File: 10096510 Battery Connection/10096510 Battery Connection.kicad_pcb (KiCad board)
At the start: 4 copper layers, 0 parts

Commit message: Replace 10096510 Battery Connection.kicad_pcb
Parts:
- added C1: 10nF, Capacitor_SMD:C_0603_1608Metric, B.Cu at (143.0, 104.5)
- added C2: 10nF, Capacitor_SMD:C_0603_1608Metric, B.Cu at (127.0, 104.5)
- added C3: 47pF, Capacitor_SMD:C_0603_1608Metric, B.Cu at (123.5, 94.5)
- added C4: 47pF, Capacitor_SMD:C_0603_1608Metric, B.Cu at (127.0, 94.5)
- added FI2: Ferrite bead, Resistor_SMD:R_0603_1608Metric, B.Cu at (123.5, 89.0)
- added FI3: Ferrite bead, Resistor_SMD:R_0603_1608Metric, B.Cu at (127.0, 89.0)
- added FL1: BNX002-01, myParts:BNX002-01, F.Cu at (135.5, 104.0)
- added J1: Conn_02x05_Odd_Even, Connector_IDC:IDC-Header_2x05_P2.54mm_Horizontal, F.Cu at (137.0, 92.0)
- added J3: +, myParts:811S100230014101, B.Cu at (108.7, 103.0)
- added J4: BAT_EEPROM, myParts:811S100230014101, B.Cu at (108.7, 107.0)
- added J5: T, myParts:811S100230014101, B.Cu at (108.7, 111.0)
- added J6: GND, myParts:GKS-913-Z, B.Cu at (108.7, 115.0)
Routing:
- net Net-(C2-Pad2): track 0.00 -> 55.4 mm
- net Net-(C2-Pad1): track 0.00 -> 51.5 mm
- net Net-(C4-Pad1): track 0.00 -> 41.8 mm
- net Net-(C1-Pad1): track 0.00 -> 29.9 mm
- net Net-(C3-Pad1): track 0.00 -> 25.5 mm
- net Net-(C1-Pad2): track 0.00 -> 22.5 mm
- net Net-(FI2-Pad2): track 0.00 -> 20.1 mm
- net Net-(FI3-Pad2): track 0.00 -> 17.0 mm
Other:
- board outline added: 68 x 45 mm
- net class HIGH CURRENT added: clearance 0.1524, trace_width 2, via_dia 0.6858, via_drill 0.3302
- board text added: "Battery Connection RB0505 10096506 Rev A"

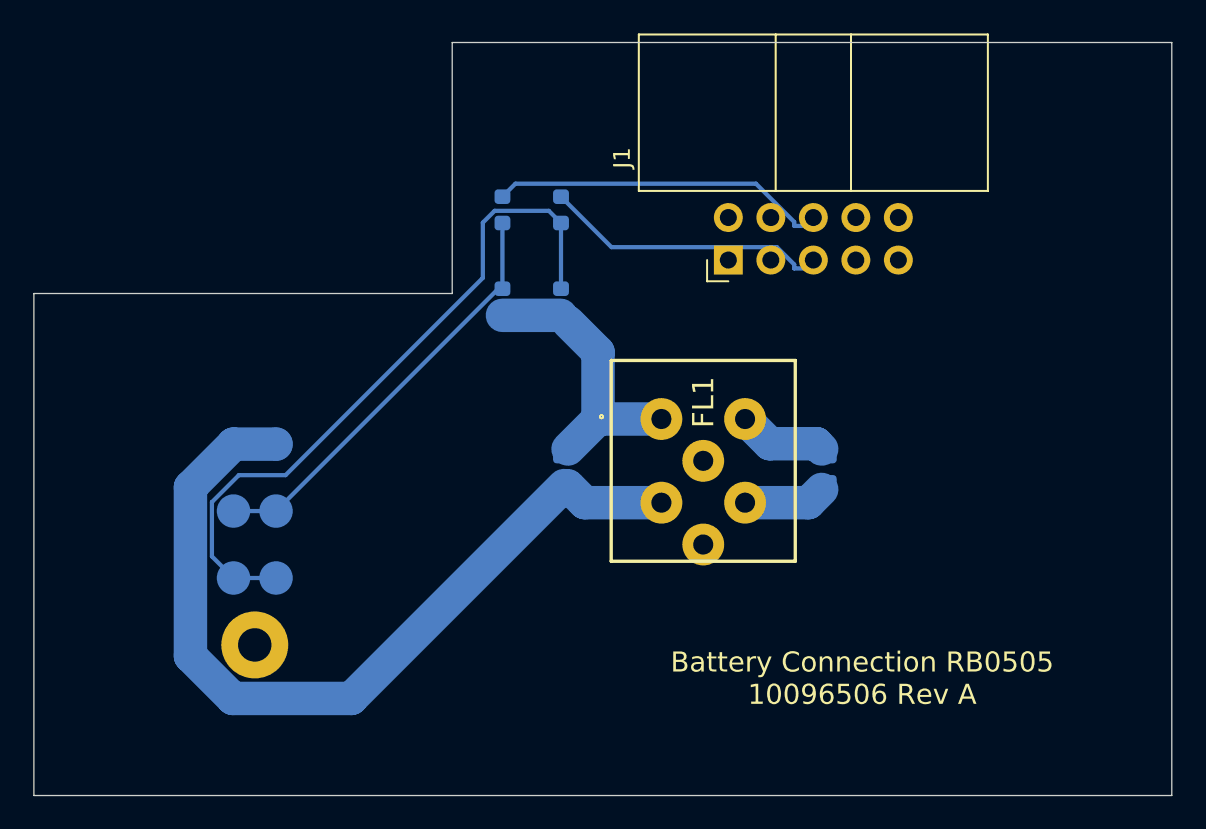
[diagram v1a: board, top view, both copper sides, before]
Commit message: Fixed missing pin 6 on BNX002-11 symbol. Updated footprint to match existing layout pin configuration for BNX002-11. Aligned components to placement on current design. Started routing. Layout still work in progress.
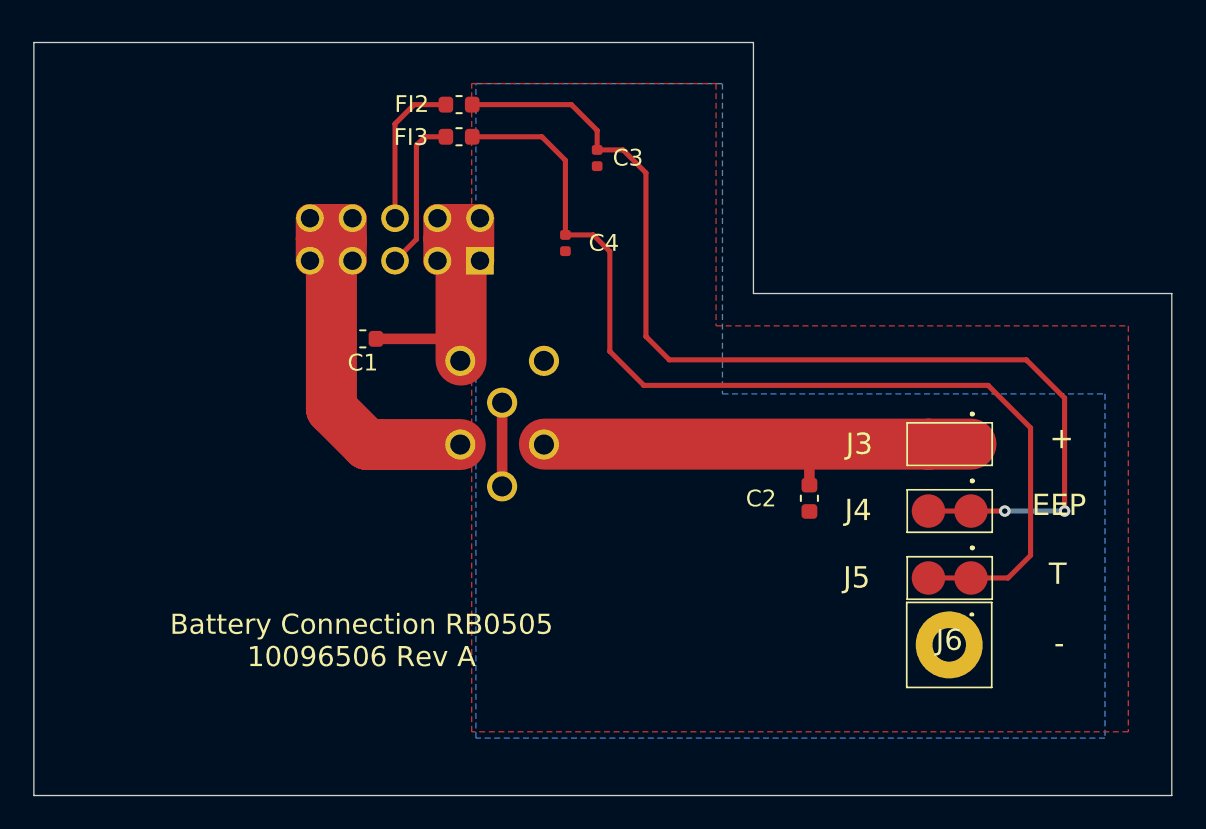
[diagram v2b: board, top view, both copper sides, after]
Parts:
- removed FL1: BNX002-01, myParts:BNX002-01
- added FI1: BNX002-11, 10096510 Battery Connection:BNX002-011, B.Cu at (123.5, 100.5)
- C1, C2: footprint Capacitor_SMD:C_0603_1608Metric -> 10096510 Battery Connection:C_0603_1608Metric; moved to F.Cu
- C3, C4: value 47pF -> 0402_47pF_C0402C470J5GAC; footprint Capacitor_SMD:C_0603_1608Metric -> 10096510 Battery Connection:C_0402_1005Metric; moved to F.Cu
- FI2, FI3: value Ferrite bead -> 74279266; footprint Resistor_SMD:R_0603_1608Metric -> 10096510 Battery Connection:L_0603_1608Metric; moved to F.Cu
- J1: value Conn_02x05_Odd_Even -> 09185107323; footprint Connector_IDC:IDC-Header_2x05_P2.54mm_Horizontal -> 10096510 Battery Connection:SHDRRA10W64P254_2X5_2050X890X930P; moved to B.Cu
- J3: value + -> 811-S1-002-30-014101; footprint myParts:811S100230014101 -> 10096510 Battery Connection:CONN_811S100230014101; moved to F.Cu
- J4: value BAT_EEPROM -> 811-S1-002-30-014101; footprint myParts:811S100230014101 -> 10096510 Battery Connection:CONN_811S100230014101; moved to F.Cu
- J5: value T -> 811-S1-002-30-014101; footprint myParts:811S100230014101 -> 10096510 Battery Connection:CONN_811S100230014101; moved to F.Cu
- J6: value GND -> GKS-913-0024; footprint myParts:GKS-913-Z -> 10096510 Battery Connection:CONN_GKS-913-Z; moved to F.Cu
- moved J3 41.5 mm to (150.2, 103.0), turned to 180 degrees
- moved J4 41.5 mm to (150.2, 107.0), turned to 180 degrees
- moved J5 41.5 mm to (150.2, 111.0), turned to 180 degrees
- moved J6 41.5 mm to (150.2, 115.0), turned to 180 degrees
- moved C1 28.9 mm to (115.2, 96.7), turned to 180 degrees
- moved C2 14.9 mm to (141.8, 106.2), turned to 270 degrees
- moved J1 14.8 mm to (122.2, 92.0), turned to 180 degrees
- moved C3 10.3 mm to (129.2, 85.9)
- moved FI3 7.50 mm to (120.9, 84.6), turned to 0 degrees
- moved FI2 6.80 mm to (120.9, 82.7), turned to 180 degrees
- moved C4 3.53 mm to (127.3, 91.0)
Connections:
- net Net-(C2-Pad1) renamed /+
- net Net-(C2-Pad2) renamed GND
- net Net-(C3-Pad1) renamed /BAT_EEPROM
- C1 pad 1: Net-(C1-Pad1) -> Earth
- C1 pad 2: Net-(C1-Pad2) -> VDD
- C4 pad 1: Net-(C4-Pad1) -> /T
- FI3 pad 1: Net-(C4-Pad1) -> Net-(FI3-Pad1)
- FI3 pad 2: Net-(FI3-Pad2) -> /T
- J1 pad 1: Net-(C1-Pad2) -> Earth
- J1 pad 10: Net-(C1-Pad1) -> VDD
- J1 pad 2: Net-(C1-Pad2) -> Earth
- J1 pad 3: Net-(C1-Pad2) -> Earth
- J1 pad 4: Net-(C1-Pad2) -> Earth
- J1 pad 5: Net-(FI3-Pad2) -> Net-(FI3-Pad1)
- J1 pad 7: Net-(C1-Pad1) -> VDD
- J1 pad 8: Net-(C1-Pad1) -> VDD
- J1 pad 9: Net-(C1-Pad1) -> VDD
- J5 pad 1: Net-(C4-Pad1) -> /T
- J5 pad 2: Net-(C4-Pad1) -> /T
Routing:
- net /T: track 0.00 -> 61.0 mm
- net GND: track 55.4 -> 5.00 mm
- net Net-(C4-Pad1): track 41.8 -> 0.00 mm
- net /BAT_EEPROM: track 25.5 -> 63.9 mm, vias 0 -> 2
- net VDD: track 0.00 -> 32.8 mm
- net Net-(C1-Pad1): track 29.9 -> 0.00 mm
- net Earth: track 0.00 -> 25.6 mm
- net Net-(C1-Pad2): track 22.5 -> 0.00 mm
- net Net-(FI3-Pad2): track 17.0 -> 0.00 mm
- net /+: track 51.5 -> 35.0 mm
- net Net-(FI2-Pad2): track 20.1 -> 9.16 mm
- net Net-(FI3-Pad1): track 0.00 -> 9.40 mm
- added copper zone on B.Cu, net GND
- added copper zone on F.Cu, net GND
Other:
- outline, holes or cut-outs redrawn
- copper layers 4 -> 2
- board text added: "+"
- board text added: "-"
- board text added: "EEP"
- board text added: "T"

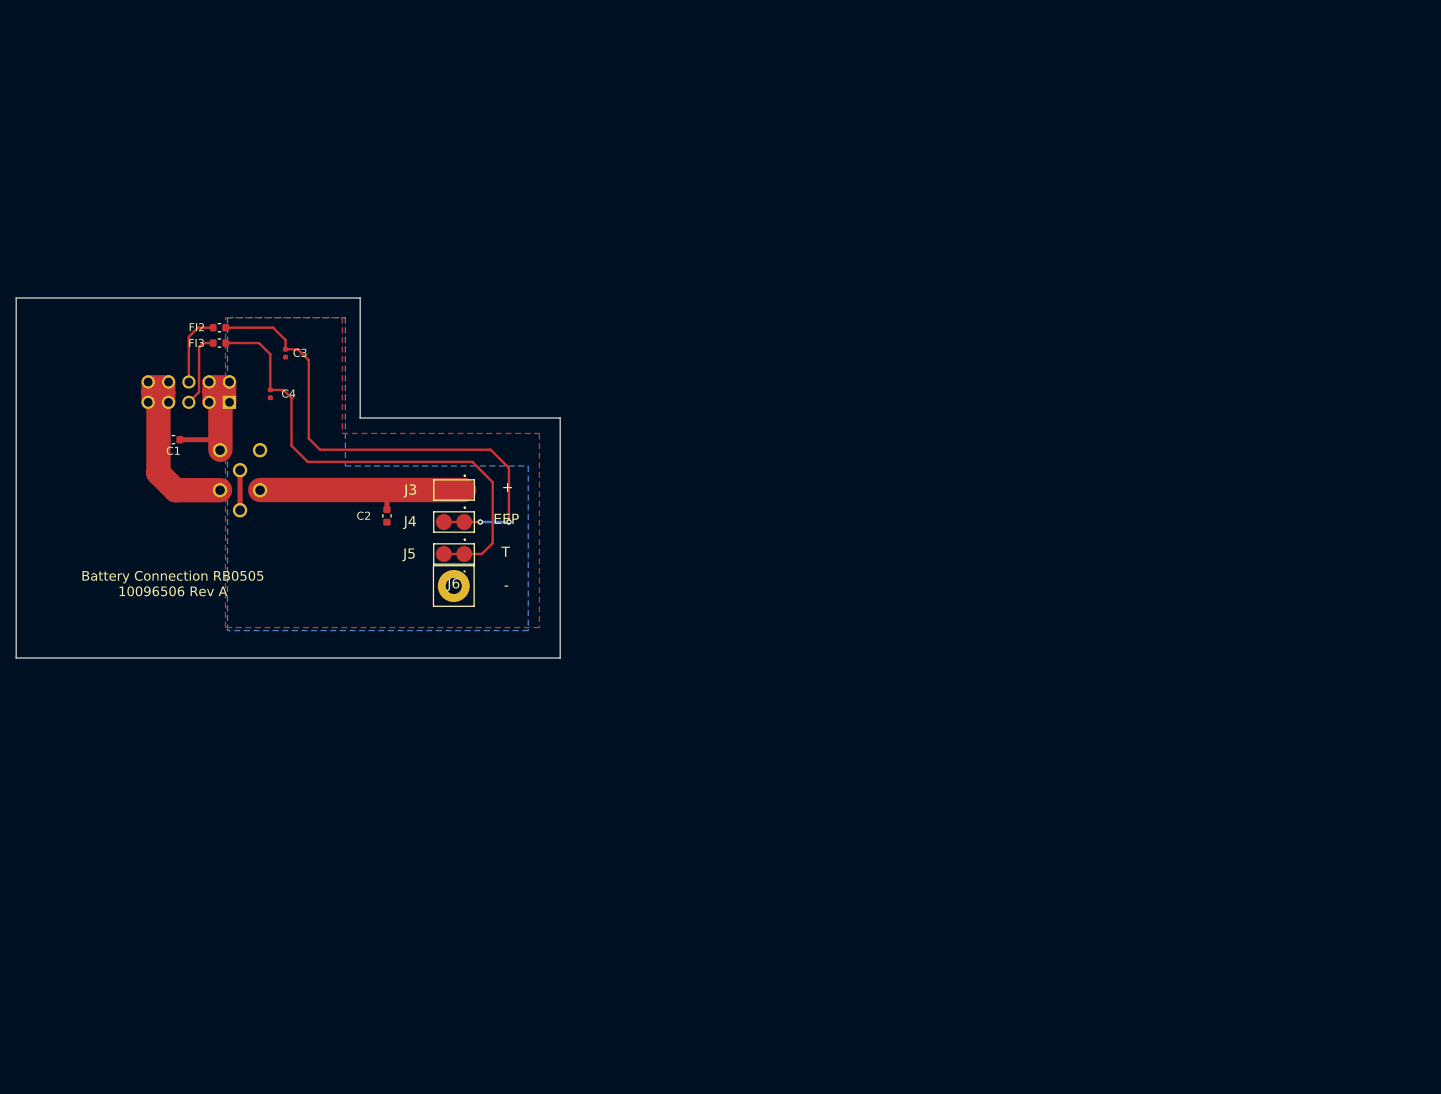
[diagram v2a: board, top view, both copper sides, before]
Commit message: Merge branch 'master' of https://gitlab.com/openventilator/openventilator into batteryconnector-dev
WIP.

Updated hole and pad sizes to match imported design files for connectors & filter and fixed filter pinout.
Added silk for label.
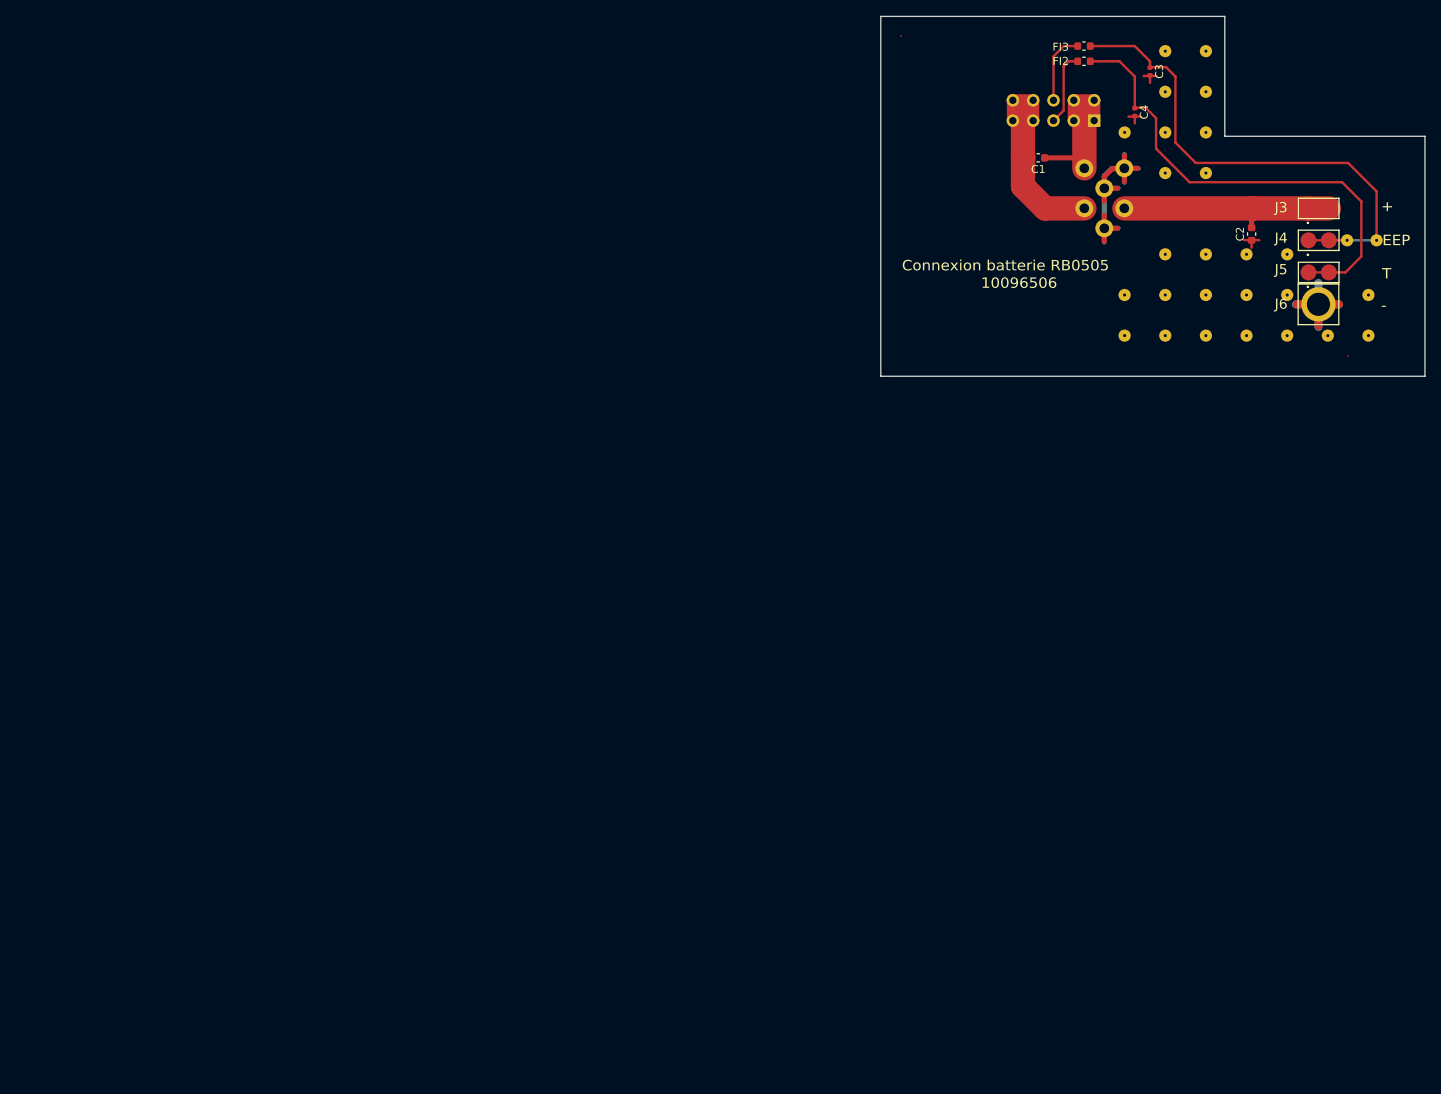
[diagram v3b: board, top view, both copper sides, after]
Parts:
- added ?: , , F.Cu at (239.1, 58.3)
- added ?: , , F.Cu at (259.5, 83.7)
- added ?: , , F.Cu at (254.4, 83.7)
- added ?: , , F.Cu at (249.3, 83.7)
- added ?: , , F.Cu at (249.3, 78.6)
- added ?: , , F.Cu at (239.1, 83.7)
- added ?: , , F.Cu at (244.2, 83.7)
- added ?: , , F.Cu at (239.1, 78.6)
- added ?: , , F.Cu at (244.2, 78.6)
- added ?: , , F.Cu at (239.1, 73.5)
- added ?: , , F.Cu at (244.2, 73.5)
- added ?: , , F.Cu at (234.1, 58.3)
- added ?: , , F.Cu at (249.3, 73.5)
- added ?: , , F.Cu at (254.4, 73.5)
- added ?: , , F.Cu at (254.4, 78.6)
- added ?: , , F.Cu at (234.1, 83.7)
- added ?: , , F.Cu at (261.9, 71.8)
- added ?: , , F.Cu at (265.5, 71.8)
- added ?: , , F.Cu at (244.2, 63.4)
- added ?: , , F.Cu at (239.1, 53.2)
- added ?: , , F.Cu at (234.1, 78.6)
- added ?: , , F.Cu at (239.1, 48.1)
- added ?: , , F.Cu at (244.2, 48.1)
- added ?: , , F.Cu at (244.2, 53.2)
- added ?: , , F.Cu at (239.1, 63.4)
- added ?: , , F.Cu at (244.2, 58.3)
- added ?: , , F.Cu at (264.5, 78.6)
- added ?: , , F.Cu at (264.5, 83.7)
- added PT1: MIRECMS, MIRECMS_D-1.5_1, F.Cu at (206.1, 46.2)
- added PT2: MIRECMS, MIRECMS_D-1.5_1, F.Cu at (262.0, 86.2)
- moved C1 113.7 mm to (223.3, 61.5)
- moved C2 113.7 mm to (249.9, 71.0), turned to 90 degrees
- moved J6 113.7 mm to (258.3, 79.8), turned to 0 degrees
- moved J1 113.7 mm to (230.2, 56.8)
- moved J4 113.7 mm to (258.3, 71.8), turned to 0 degrees
- moved J3 113.7 mm to (258.3, 67.8), turned to 0 degrees
- moved J5 113.7 mm to (258.3, 75.8), turned to 0 degrees
- moved C3 113.7 mm to (237.2, 50.7)
- moved FI3 113.7 mm to (229.0, 49.4)
- moved FI2 113.7 mm to (229.0, 47.5)
- moved C4 113.7 mm to (235.3, 55.8)
- moved FI1 113.6 mm to (231.5, 65.3)
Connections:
- C2 pad 1: /+ -> GND
- C2 pad 2: GND -> /+
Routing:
- net GND: track 5.00 -> 90.5 mm
- net /+: track 35.0 -> 28.0 mm
- net Earth: track 25.6 -> 23.8 mm
- net /T: track 61.0 -> 59.9 mm
- net VDD: track 32.8 -> 32.0 mm
- net /BAT_EEPROM: track 63.9 -> 63.4 mm, vias 2 -> 0
- removed copper zone on B.Cu, net GND
- removed copper zone on F.Cu, net GND
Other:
- net class Default: clearance 0.1524 -> 0.2; trace_width 0.254 -> 0.25; via_dia 0.6858 -> 0.8; via_drill 0.3302 -> 0.4
- net class HIGH CURRENT removed
- rule pad_to_mask_clearance: 0 -> 0.051
- rule solder_mask_min_width: 0.1016 -> 0.25
- rule trace_clearance: 0.1524 -> 0.2
- rule trace_min: 0.127 -> 0.2
- rule via_min_drill: 0.254 -> 0.3
- rule via_min_size: 0.4572 -> 0.4
- board text added: "0,4"
- board text added: "0,9"
- board text added: "1,2"
- board text added: "10096506"
- board text added: "2,9"
- board text added: "ATTENTION: WARNING:"
- board text added: "Connexion batterie RB0505"
- board text added: "Fabrique suivant IPC A610 classe III. Manufactured according to IPC A610 class III."
- board text added: "Le circuit imprime doit etre UL94V-0. The printed circuit board must be UL94V-0. Le fabricant doit etre reconnu UL et doit apposer le marquage correspondant. The manufacturer must be recognized UL and must affix corresponding marking."
- board text removed: "Battery Connection RB0505 10096506 Rev A"
